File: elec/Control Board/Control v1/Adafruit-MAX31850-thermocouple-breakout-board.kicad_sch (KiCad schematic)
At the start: 32 parts

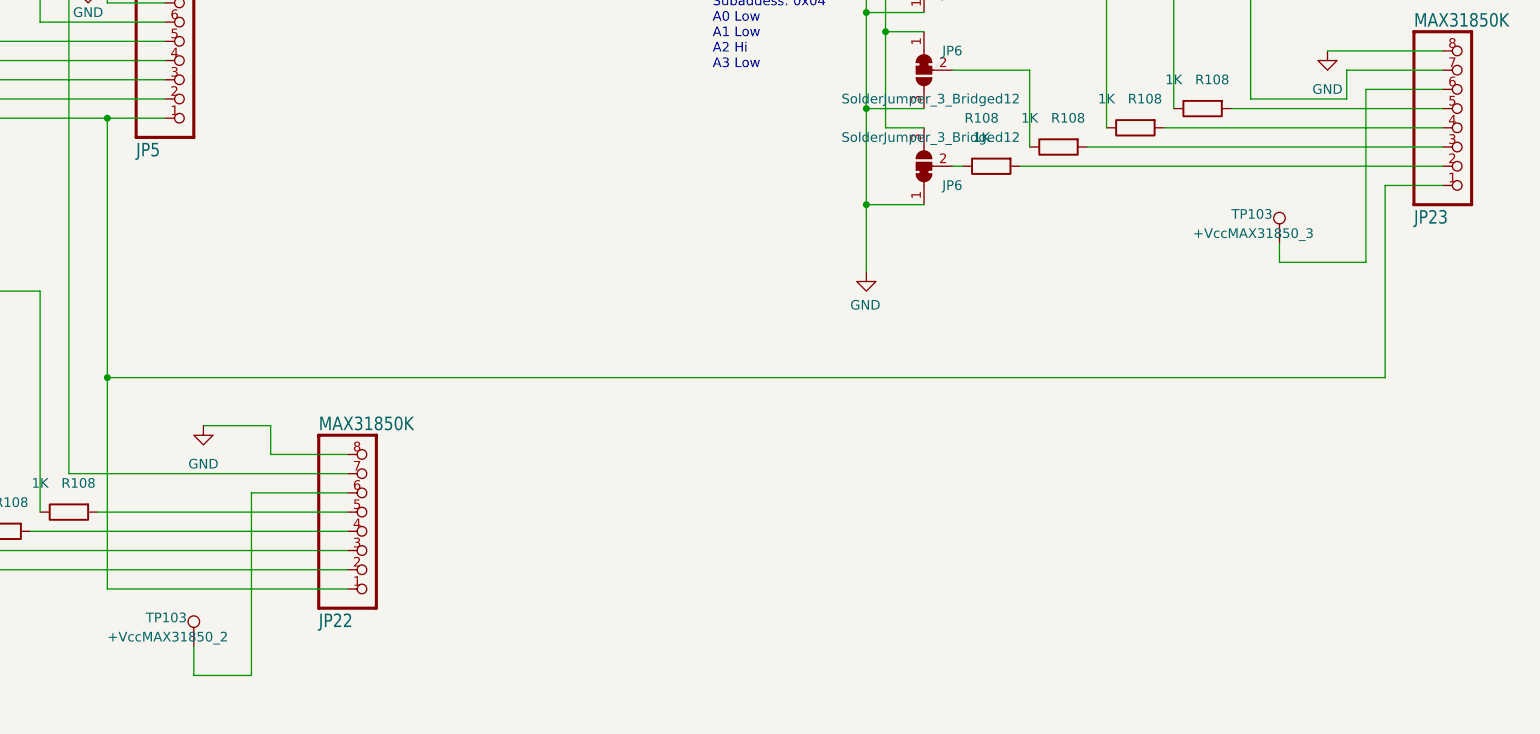
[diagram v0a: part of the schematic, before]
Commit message: More update schematic for MCP9600 I2C thermocouple.
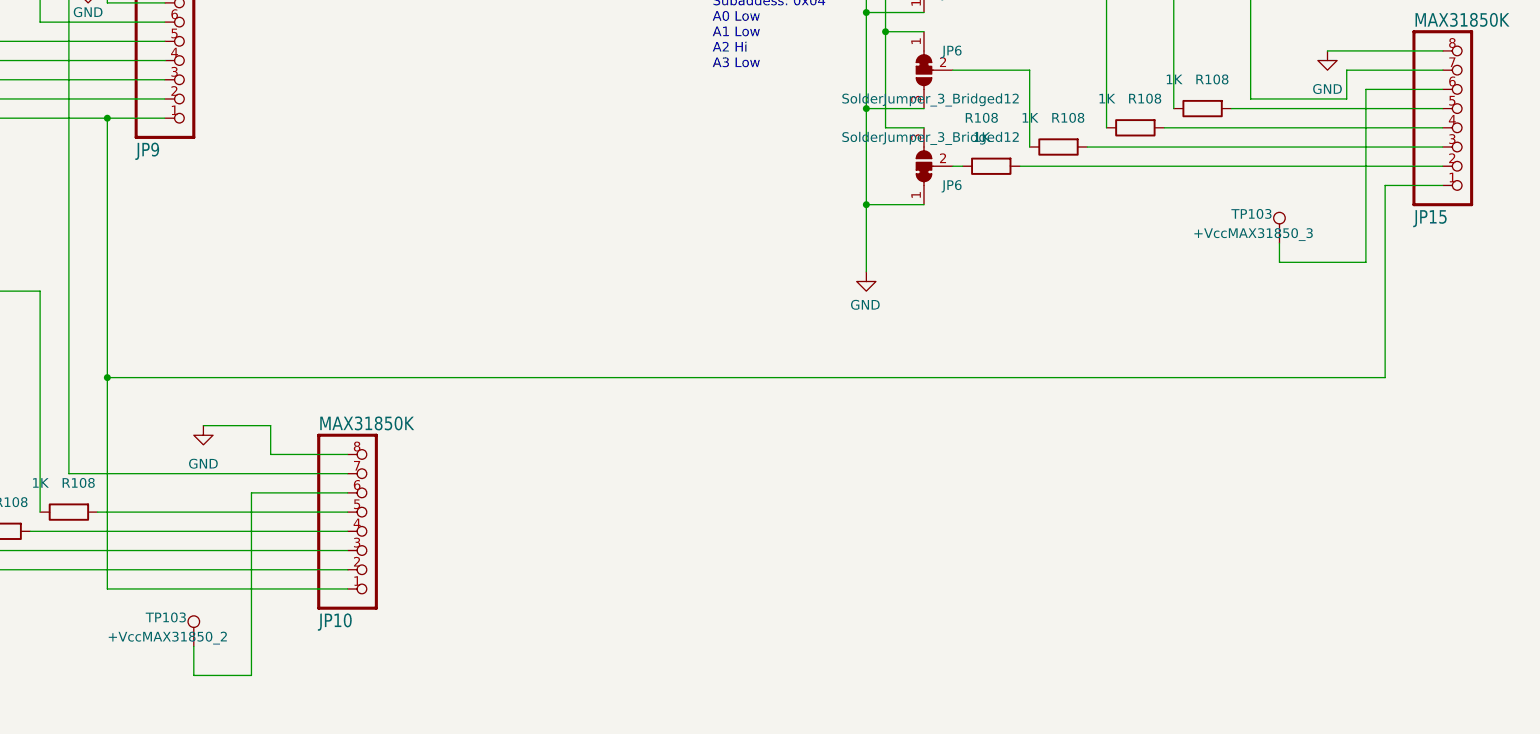
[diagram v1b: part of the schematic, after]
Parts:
- renumbered JP22 to JP10, JP23 to JP15, JP5 to JP9
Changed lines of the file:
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@@
         )
         (path "/c68c9deb-8d4d-42f0-adf8-4d3022f4ee59/3ff32a52-b1ed-4756-8661-90a95f721605"
-          (reference "JP20") (unit 1)
+          (reference "JP13") (unit 1)
         )
       )
@@
         )
         (path "/c68c9deb-8d4d-42f0-adf8-4d3022f4ee59/3ff32a52-b1ed-4756-8661-90a95f721605"
-          (reference "#PWR022") (unit 1)
+          (reference "#PWR024") (unit 1)
         )
       )
@@
         )
         (path "/c68c9deb-8d4d-42f0-adf8-4d3022f4ee59/3ff32a52-b1ed-4756-8661-90a95f721605"
-          (reference "R62") (unit 1)
+          (reference "R18") (unit 1)
         )
       )
@@
         )
         (path "/c68c9deb-8d4d-42f0-adf8-4d3022f4ee59/3ff32a52-b1ed-4756-8661-90a95f721605"
-          (reference "R61") (unit 1)
+          (reference "R17") (unit 1)
         )
       )
@@
         )
         (path "/c68c9deb-8d4d-42f0-adf8-4d3022f4ee59/3ff32a52-b1ed-4756-8661-90a95f721605"
-          (reference "R59") (unit 1)
+          (reference "R15") (unit 1)
         )
       )
@@
         )
         (path "/c68c9deb-8d4d-42f0-adf8-4d3022f4ee59/3ff32a52-b1ed-4756-8661-90a95f721605"
-          (reference "R10") (unit 1)
+          (reference "R11") (unit 1)
         )
       )
@@
         )
         (path "/c68c9deb-8d4d-42f0-adf8-4d3022f4ee59/3ff32a52-b1ed-4756-8661-90a95f721605"
-          (reference "JP14") (unit 1)
+          (reference "JP5") (unit 1)
         )
       )
@@
         )
         (path "/c68c9deb-8d4d-42f0-adf8-4d3022f4ee59/3ff32a52-b1ed-4756-8661-90a95f721605"
-          (reference "JP19") (unit 1)
+          (reference "JP12") (unit 1)
         )
       )
@@
       (project "Control v1"
         (path "/c68c9deb-8d4d-42f0-adf8-4d3022f4ee59/3ff32a52-b1ed-4756-8661-90a95f721605"
-          (reference "TP11") (unit 1)
+          (reference "TP3") (unit 1)
         )
       )
@@
         )
         (path "/c68c9deb-8d4d-42f0-adf8-4d3022f4ee59/3ff32a52-b1ed-4756-8661-90a95f721605"
-          (reference "R58") (unit 1)
+          (reference "R14") (unit 1)
         )
       )
@@
   (symbol (lib_id "Control v1-eagle-import:microbuilder_HEADER-1X870MIL") (at 110.49 91.44 0) (mirror x) (unit 1)
     (in_bom yes) (on_board yes) (dnp no)
-    (property "Reference" "JP5" (at 104.14 104.775 0)
+    (property "Reference" "JP9" (at 104.14 104.775 0)
       (effects (font (size 1.778 1.5113)) (justify left bottom))
     )
@@
       (project "Control v1"
         (path "/c68c9deb-8d4d-42f0-adf8-4d3022f4ee59/3ff32a52-b1ed-4756-8661-90a95f721605"
-          (reference "JP5") (unit 1)
+          (reference "JP9") (unit 1)
         )
       )
@@
         )
         (path "/c68c9deb-8d4d-42f0-adf8-4d3022f4ee59/3ff32a52-b1ed-4756-8661-90a95f721605"
-          (reference "R7") (unit 1)
+          (reference "R6") (unit 1)
         )
       )
@@
       (project "Control v1"
         (path "/c68c9deb-8d4d-42f0-adf8-4d3022f4ee59/3ff32a52-b1ed-4756-8661-90a95f721605"
-          (reference "TP12") (unit 1)
+          (reference "TP4") (unit 1)
         )
       )
@@
         )
         (path "/c68c9deb-8d4d-42f0-adf8-4d3022f4ee59/3ff32a52-b1ed-4756-8661-90a95f721605"
-          (reference "JP18") (unit 1)
+          (reference "JP11") (unit 1)
         )
       )
@@
         )
         (path "/c68c9deb-8d4d-42f0-adf8-4d3022f4ee59/3ff32a52-b1ed-4756-8661-90a95f721605"
-          (reference "R60") (unit 1)
+          (reference "R16") (unit 1)
         )
       )
@@
         )
         (path "/c68c9deb-8d4d-42f0-adf8-4d3022f4ee59/3ff32a52-b1ed-4756-8661-90a95f721605"
-          (reference "R57") (unit 1)
+          (reference "R13") (unit 1)
         )
       )
@@
         )
         (path "/c68c9deb-8d4d-42f0-adf8-4d3022f4ee59/3ff32a52-b1ed-4756-8661-90a95f721605"
-          (reference "#PWR024") (unit 1)
+          (reference "#PWR025") (unit 1)
         )
       )
@@
   (symbol (lib_id "Control v1-eagle-import:microbuilder_HEADER-1X870MIL") (at 134.62 153.67 0) (mirror x) (unit 1)
     (in_bom yes) (on_board yes) (dnp no)
-    (property "Reference" "JP22" (at 128.27 167.005 0)
+    (property "Reference" "JP10" (at 128.27 167.005 0)
       (effects (font (size 1.778 1.5113)) (justify left bottom))
     )
@@
       (project "Control v1"
         (path "/c68c9deb-8d4d-42f0-adf8-4d3022f4ee59/3ff32a52-b1ed-4756-8661-90a95f721605"
-          (reference "JP22") (unit 1)
+          (reference "JP10") (unit 1)
         )
       )
@@
   (symbol (lib_id "Control v1-eagle-import:microbuilder_HEADER-1X870MIL") (at 279.4 100.33 0) (mirror x) (unit 1)
     (in_bom yes) (on_board yes) (dnp no)
-    (property "Reference" "JP23" (at 273.05 113.665 0)
+    (property "Reference" "JP15" (at 273.05 113.665 0)
       (effects (font (size 1.778 1.5113)) (justify left bottom))
     )
@@
       (project "Control v1"
         (path "/c68c9deb-8d4d-42f0-adf8-4d3022f4ee59/3ff32a52-b1ed-4756-8661-90a95f721605"
-          (reference "JP23") (unit 1)
+          (reference "JP15") (unit 1)
         )
       )
@@
         )
         (path "/c68c9deb-8d4d-42f0-adf8-4d3022f4ee59/3ff32a52-b1ed-4756-8661-90a95f721605"
-          (reference "JP16") (unit 1)
+          (reference "JP7") (unit 1)
         )
       )
@@
         )
         (path "/c68c9deb-8d4d-42f0-adf8-4d3022f4ee59/3ff32a52-b1ed-4756-8661-90a95f721605"
-          (reference "JP21") (unit 1)
+          (reference "JP14") (unit 1)
         )
       )
@@
         )
         (path "/c68c9deb-8d4d-42f0-adf8-4d3022f4ee59/3ff32a52-b1ed-4756-8661-90a95f721605"
-          (reference "JP15") (unit 1)
+          (reference "JP6") (unit 1)
         )
       )
@@
         )
         (path "/c68c9deb-8d4d-42f0-adf8-4d3022f4ee59/3ff32a52-b1ed-4756-8661-90a95f721605"
-          (reference "#PWR03") (unit 1)
+          (reference "#PWR021") (unit 1)
         )
       )
@@
         )
         (path "/c68c9deb-8d4d-42f0-adf8-4d3022f4ee59/3ff32a52-b1ed-4756-8661-90a95f721605"
-          (reference "R56") (unit 1)
+          (reference "R12") (unit 1)
         )
       )
@@
         )
         (path "/c68c9deb-8d4d-42f0-adf8-4d3022f4ee59/3ff32a52-b1ed-4756-8661-90a95f721605"
-          (reference "JP17") (unit 1)
+          (reference "JP8") (unit 1)
         )
       )
@@
         )
         (path "/c68c9deb-8d4d-42f0-adf8-4d3022f4ee59/3ff32a52-b1ed-4756-8661-90a95f721605"
-          (reference "R55") (unit 1)
+          (reference "R10") (unit 1)
         )
       )
@@
         )
         (path "/c68c9deb-8d4d-42f0-adf8-4d3022f4ee59/3ff32a52-b1ed-4756-8661-90a95f721605"
-          (reference "R6") (unit 1)
+          (reference "R7") (unit 1)
         )
       )
@@
         )
         (path "/c68c9deb-8d4d-42f0-adf8-4d3022f4ee59/3ff32a52-b1ed-4756-8661-90a95f721605"
-          (reference "#PWR021") (unit 1)
-        )
-      )
+          (reference "#PWR022") (unit 1)
+        )
+      )

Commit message: Fix swome ERC errors.
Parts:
- removed JP9: MAX31850K, PubInv_KiCad_PCB:Adafruit_MAX31850K_Module, symbol Control v1-eagle-import:microbuilder_HEADER-1X870MIL
- added J2: MAX31850K, PubInv_KiCad_PCB:Adafruit_MAX31850K_Module, symbol Connector_Generic:Conn_01x08
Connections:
- net +VccMAX31850: now also J2.7 (Pin_7)
- net DATA: now also J2.1 (Pin_1)
- net GND: now also J2.8 (Pin_8)
- net at R108.2: now also J2.5 (Pin_5)
- net at R108.2: now also J2.2 (Pin_2)
- net at R108.2: now also J2.3 (Pin_3)
- net at R108.2: now also J2.4 (Pin_4)
- net at TP103.1: now also J2.6 (Pin_6)
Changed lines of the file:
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@@
         )
         (path "/c68c9deb-8d4d-42f0-adf8-4d3022f4ee59/3ff32a52-b1ed-4756-8661-90a95f721605"
-          (reference "#PWR024") (unit 1)
+          (reference "#PWR033") (unit 1)
         )
       )
@@
         )
         (path "/c68c9deb-8d4d-42f0-adf8-4d3022f4ee59/3ff32a52-b1ed-4756-8661-90a95f721605"
-          (reference "R18") (unit 1)
+          (reference "R26") (unit 1)
         )
       )
@@
         )
         (path "/c68c9deb-8d4d-42f0-adf8-4d3022f4ee59/3ff32a52-b1ed-4756-8661-90a95f721605"
-          (reference "R17") (unit 1)
+          (reference "R25") (unit 1)
         )
       )
@@
         )
         (path "/c68c9deb-8d4d-42f0-adf8-4d3022f4ee59/3ff32a52-b1ed-4756-8661-90a95f721605"
-          (reference "R15") (unit 1)
+          (reference "R23") (unit 1)
         )
       )
@@
       (project "Control v1"
         (path "/c68c9deb-8d4d-42f0-adf8-4d3022f4ee59/3ff32a52-b1ed-4756-8661-90a95f721605"
-          (reference "TP1") (unit 1)
+          (reference "TP2") (unit 1)
         )
       )
@@
         )
         (path "/c68c9deb-8d4d-42f0-adf8-4d3022f4ee59/3ff32a52-b1ed-4756-8661-90a95f721605"
-          (reference "R11") (unit 1)
+          (reference "R19") (unit 1)
         )
       )
@@
       (project "Control v1"
         (path "/c68c9deb-8d4d-42f0-adf8-4d3022f4ee59/3ff32a52-b1ed-4756-8661-90a95f721605"
-          (reference "TP3") (unit 1)
+          (reference "TP4") (unit 1)
         )
       )
@@
         )
         (path "/c68c9deb-8d4d-42f0-adf8-4d3022f4ee59/3ff32a52-b1ed-4756-8661-90a95f721605"
-          (reference "R14") (unit 1)
-        )
-      )
-    )
-  )
-  (symbol (lib_id "Control v1-eagle-import:microbuilder_HEADER-1X870MIL") (at 110.49 91.44 0) (mirror x) (unit 1)
-    (in_bom yes) (on_board yes) (dnp no)
-    (property "Reference" "JP9" (at 104.14 104.775 0)
-      (effects (font (size 1.778 1.5113)) (justify left bottom))
-    )
-    (property "Value" "MAX31850K" (at 104.14 78.74 0)
-      (effects (font (size 1.778 1.5113)) (justify left bottom))
-    )
-    (property "Footprint" "PubInv_KiCad_PCB:Adafruit_MAX31850K_Module" (at 110.49 91.44 0)
-      (effects (font (size 1.27 1.27)) hide)
-    )
-    (property "Datasheet" "" (at 110.49 91.44 0)
+          (reference "R22") (unit 1)
+        )
+      )
+    )
+  )
+  (symbol (lib_id "Connector_Generic:Conn_01x08") (at 113.03 93.98 0) (mirror x) (unit 1)
+    (in_bom yes) (on_board yes) (dnp no)
+    (property "Reference" "J2" (at 113.03 77.47 0)
+      (effects (font (size 1.27 1.27)))
+    )
+    (property "Value" "MAX31850K" (at 113.03 80.01 0)
+      (effects (font (size 1.27 1.27)))
+    )
+    (property "Footprint" "PubInv_KiCad_PCB:Adafruit_MAX31850K_Module" (at 113.03 93.98 0)
+      (effects (font (size 1.27 1.27)) hide)
+    )
+    (property "Datasheet" "~" (at 113.03 93.98 0)
       (effects (font (size 1.27 1.27)) hide)
     )
@@
     (instances
       (project "Control v1"
+        (path "/c68c9deb-8d4d-42f0-adf8-4d3022f4ee59"
+          (reference "J2") (unit 1)
+        )
         (path "/c68c9deb-8d4d-42f0-adf8-4d3022f4ee59/3ff32a52-b1ed-4756-8661-90a95f721605"
           (reference "JP9") (unit 1)
-        )
-      )
-      (project "Control v1"
-        (path "/f971cfba-4cca-4938-b098-1d0ea8f2906e"
-          (reference "JP1") (unit 1)
         )
       )
@@
         )
         (path "/c68c9deb-8d4d-42f0-adf8-4d3022f4ee59/3ff32a52-b1ed-4756-8661-90a95f721605"
-          (reference "R6") (unit 1)
+          (reference "R14") (unit 1)
         )
       )
@@
       (project "Control v1"
         (path "/c68c9deb-8d4d-42f0-adf8-4d3022f4ee59/3ff32a52-b1ed-4756-8661-90a95f721605"
-          (reference "TP4") (unit 1)
+          (reference "TP5") (unit 1)
         )
       )
@@
         )
         (path "/c68c9deb-8d4d-42f0-adf8-4d3022f4ee59/3ff32a52-b1ed-4756-8661-90a95f721605"
-          (reference "R9") (unit 1)
+          (reference "R17") (unit 1)
         )
       )
@@
         )
         (path "/c68c9deb-8d4d-42f0-adf8-4d3022f4ee59/3ff32a52-b1ed-4756-8661-90a95f721605"
-          (reference "R16") (unit 1)
+          (reference "R24") (unit 1)
         )
       )
@@
         )
         (path "/c68c9deb-8d4d-42f0-adf8-4d3022f4ee59/3ff32a52-b1ed-4756-8661-90a95f721605"
-          (reference "R13") (unit 1)
+          (reference "R21") (unit 1)
         )
       )
@@
         )
         (path "/c68c9deb-8d4d-42f0-adf8-4d3022f4ee59/3ff32a52-b1ed-4756-8661-90a95f721605"
-          (reference "#PWR025") (unit 1)
+          (reference "#PWR034") (unit 1)
         )
       )
@@
         )
         (path "/c68c9deb-8d4d-42f0-adf8-4d3022f4ee59/3ff32a52-b1ed-4756-8661-90a95f721605"
-          (reference "#PWR020") (unit 1)
+          (reference "#PWR029") (unit 1)
         )
       )
@@
       (project "Control v1"
         (path "/c68c9deb-8d4d-42f0-adf8-4d3022f4ee59/3ff32a52-b1ed-4756-8661-90a95f721605"
-          (reference "TP2") (unit 1)
+          (reference "TP3") (unit 1)
         )
       )
@@
         )
         (path "/c68c9deb-8d4d-42f0-adf8-4d3022f4ee59/3ff32a52-b1ed-4756-8661-90a95f721605"
-          (reference "#PWR023") (unit 1)
+          (reference "#PWR032") (unit 1)
         )
       )
@@
         )
         (path "/c68c9deb-8d4d-42f0-adf8-4d3022f4ee59/3ff32a52-b1ed-4756-8661-90a95f721605"
-          (reference "#PWR021") (unit 1)
+          (reference "#PWR030") (unit 1)
         )
       )
@@
         )
         (path "/c68c9deb-8d4d-42f0-adf8-4d3022f4ee59/3ff32a52-b1ed-4756-8661-90a95f721605"
-          (reference "R8") (unit 1)
+          (reference "R16") (unit 1)
         )
       )
@@
         )
         (path "/c68c9deb-8d4d-42f0-adf8-4d3022f4ee59/3ff32a52-b1ed-4756-8661-90a95f721605"
-          (reference "R12") (unit 1)
+          (reference "R20") (unit 1)
         )
       )
@@
         )
         (path "/c68c9deb-8d4d-42f0-adf8-4d3022f4ee59/3ff32a52-b1ed-4756-8661-90a95f721605"
-          (reference "R10") (unit 1)
+          (reference "R18") (unit 1)
         )
       )
@@
         )
         (path "/c68c9deb-8d4d-42f0-adf8-4d3022f4ee59/3ff32a52-b1ed-4756-8661-90a95f721605"
-          (reference "R7") (unit 1)
+          (reference "R15") (unit 1)
         )
       )
@@
         )
         (path "/c68c9deb-8d4d-42f0-adf8-4d3022f4ee59/3ff32a52-b1ed-4756-8661-90a95f721605"
-          (reference "#PWR022") (unit 1)
-        )
-      )
+          (reference "#PWR031") (unit 1)
+        )
+      )
